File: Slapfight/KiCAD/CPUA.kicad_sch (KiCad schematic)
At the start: 13 parts, among them U8M RAM_2016, U8N 27C256 - A77-01-1, U8P 27C256 - A77-00-1, U8Q Z80M (MAIN CPU), U9A_ 74LS08, U9J 74LS259, U9K 74LS138, U9L 74LS367, U9L_ 74LS32, U9M_ 74LS32, U9N_ 74LS14, U9P_ 74LS139

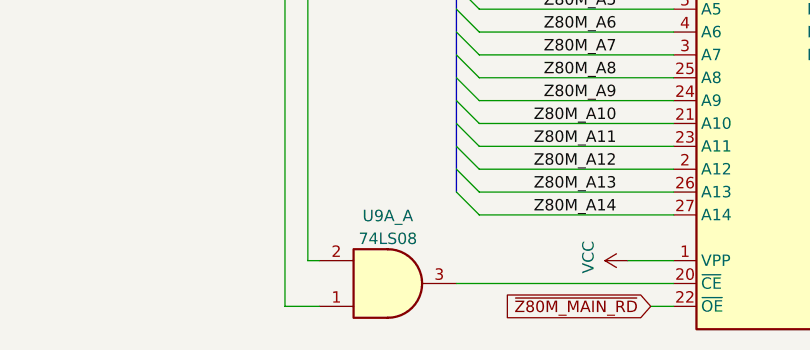
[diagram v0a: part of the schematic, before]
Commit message: Component naming updates
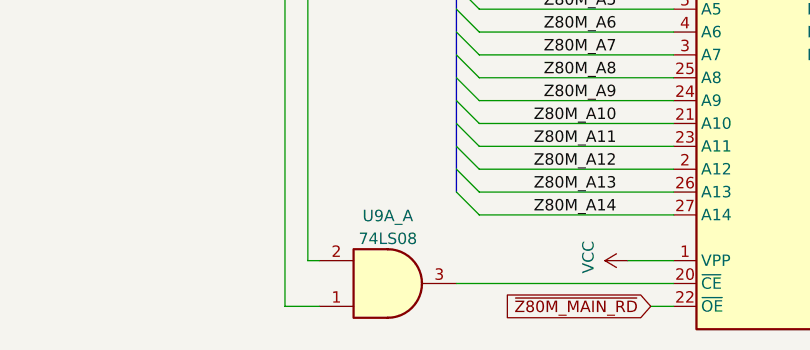
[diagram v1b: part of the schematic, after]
